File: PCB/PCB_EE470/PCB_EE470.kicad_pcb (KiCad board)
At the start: 2 copper layers, 68.6 x 53.4 mm, 25 parts, among them IC1 LME49860MAX_NOPB, J1 Power, J2 Digital/PWM, J3 Analog, J4 Digital/PWM

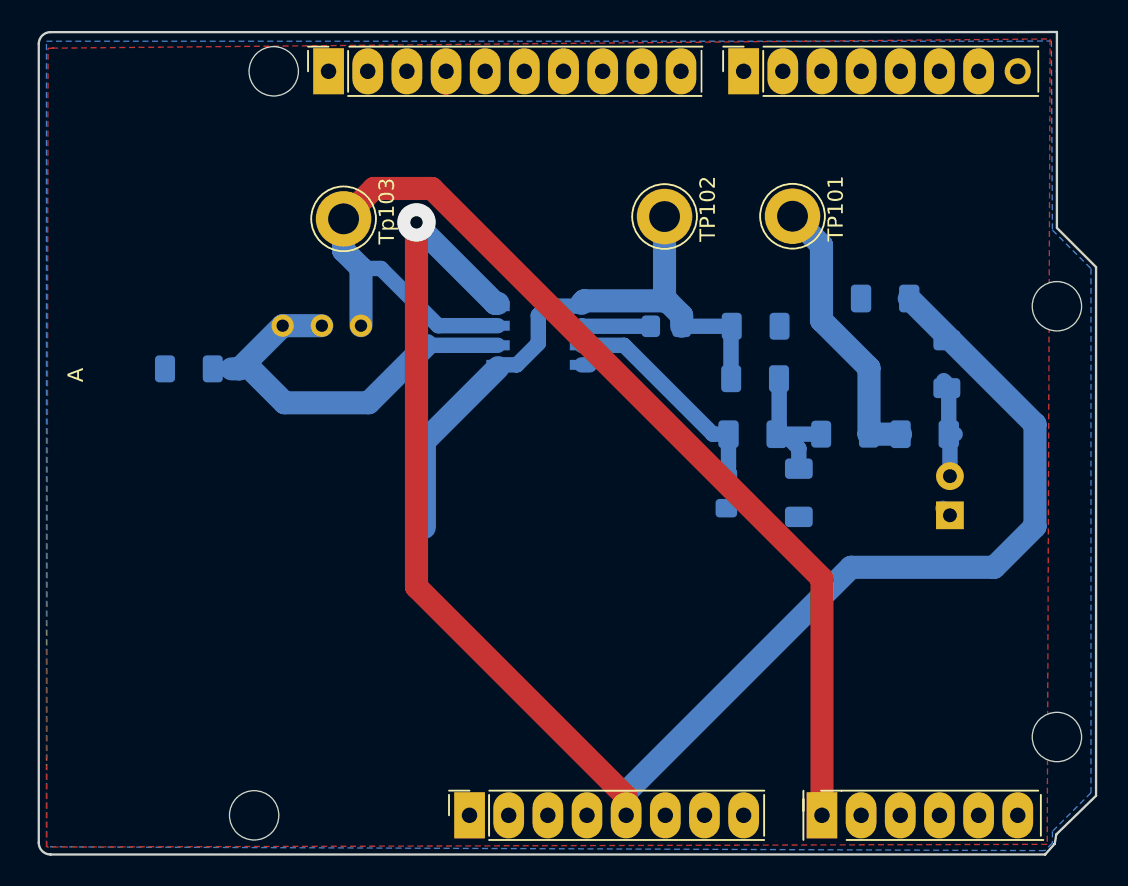
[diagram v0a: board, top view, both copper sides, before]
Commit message: ajout port jst écran arduino
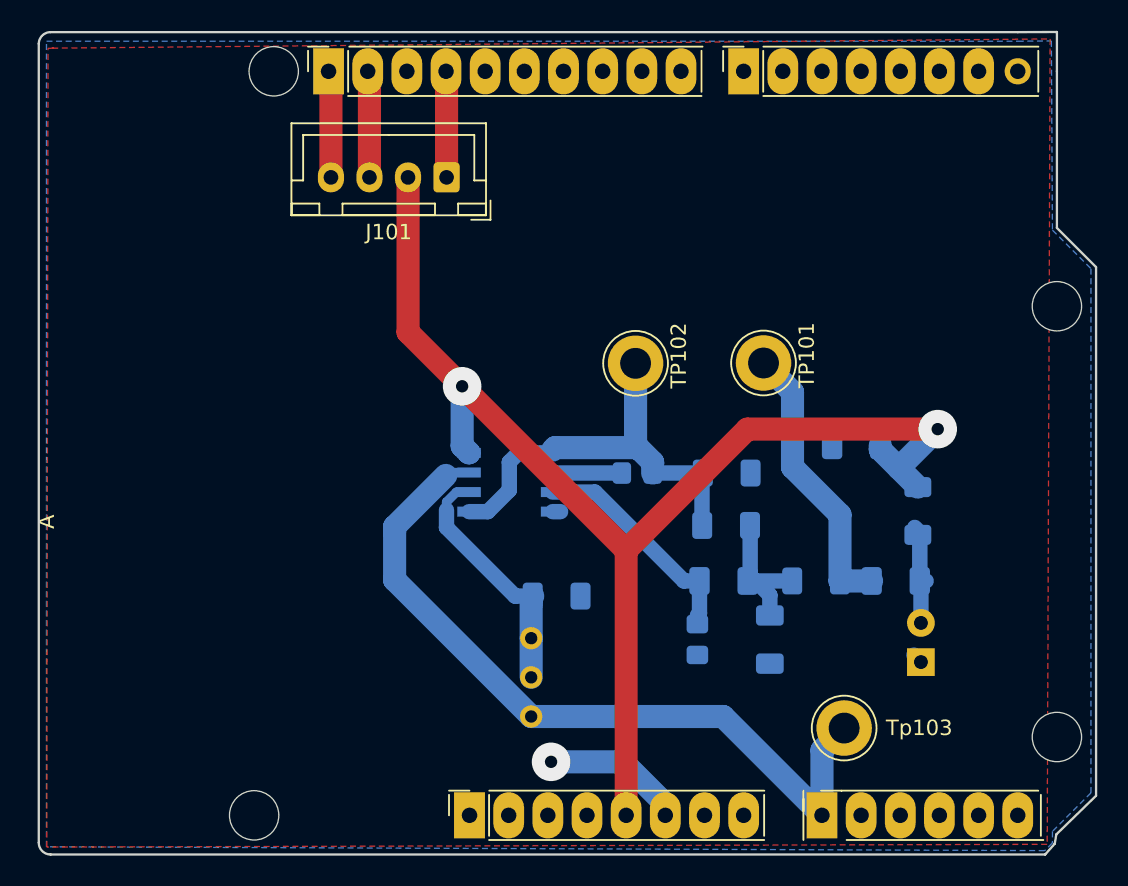
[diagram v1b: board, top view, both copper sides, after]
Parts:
- added J101: Conn_01x04_Female, Connector_JST:JST_XH_B4B-XH-A_1x04_P2.50mm_Vertical, F.Cu at (126.5, 56.1)
- moved Tp103 46.3 mm to (152.2, 91.8), turned to 0 degrees
- moved R7 28.0 mm to (133.6, 83.2), turned to 180 degrees
- moved R6 27.6 mm to (131.9, 91.0), turned to 0 degrees
- moved C2 9.70 mm to (147.4, 86.1)
- moved R2 9.70 mm to (142.7, 86.1)
- moved TP101 9.70 mm to (147.0, 68.1)
- moved TP102 9.70 mm to (138.7, 68.1)
- moved C1 9.70 mm to (144.4, 82.3)
- moved R1 9.70 mm to (150.4, 82.3)
- moved C3 9.70 mm to (155.6, 82.3)
- moved C4 9.70 mm to (153.0, 73.5)
- moved IC1 9.70 mm to (130.6, 75.9)
- moved MK1 9.70 mm to (157.2, 87.5)
- moved R3 9.70 mm to (144.6, 75.3)
- moved R4 9.70 mm to (144.6, 78.7)
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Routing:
- net /A0: track 75.5 -> 52.4 mm
- net +5V: track 106.0 -> 83.5 mm, vias 1 -> 2
- net GND: track 1.95 -> 18.1 mm, vias 0 -> 1
- net Net-(IC1-INVERTING_INPUT_B): track 31.6 -> 16.1 mm
- net /Out_Etage_1: track 39.7 -> 27.4 mm
- net /SCL/A5: track 0.00 -> 6.94 mm
- net /SDA/A4: track 0.00 -> 6.93 mm
